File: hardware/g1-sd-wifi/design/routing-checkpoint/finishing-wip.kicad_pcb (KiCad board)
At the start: 6 copper layers, 59 x 115 mm, 351 parts, among them J10 FPGA JTAG pogo pads, J20 5V/GND direct wire pads, J201 microSD push-pull 1.42mm, J202 RP USB service pads, J203 RP SWD/reset/boot pads, J204 C5 direct UART recovery pads, J40 FH12-14S-0.5SH(55), J41 FH12-6S-0.5SH(55), J50 FH12-20S-0.5SH(55), J51 FH12-20S-0.5SH(55), K201 C5 removable compression cont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, K202 C5 removable compression cont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, K203 C5 removable compression cont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, K204 C5 removable compression cont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, K205 C5 removable compression cont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, K206 C5 removable compression cont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, K207 C5 removable compression cont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, K208 C5 removable compression cont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, K209 C5 removable compression cont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, K210 C5 removable compression cont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, K211 C5 removable compression cont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, K212 C5 removable compression cont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, K213 C5 removable compression cont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, K214 C5 removable compression cont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, K215 C5 removable compression cont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, K216 C5 removable compression cont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, Q20 PMV48XP reverse polarity, Q201 C5 recovery pull-down, Q202 C5 recovery pull-down, U10 LCMXO2-2000HC-4TG100C, U20 TPS2116 automatic mux, U201 RP2350B, U202 16MiB boot NOR, U203 8MiB QSPI PSRAM, U204 C5 off-state isolation, U205 C5 off-state isolation, U207 SD4-bit DAT rail isolation, U208 SD CLK/CMD rail isolation, U209 SD enable/power-good NAND, U21 TPS62162 3.3V 1A, U22 TPS62162 3.3V 1A, U23 TPS3808G33DBVR, U24 TPS3808G33DBVR, U25 TPS3808G33DBVR, U26 TPS3808G01DBVR, U27 SN74LVC2G08DCUR, U28 SN74LVC2G08DCUR, U29 SN74LVC2G08DCUR, U30 SN74LVC1G11DBVR, U31 SN74LVC2G04DBVT, U32 SN74LVC1G32DBVR, U33 SN74LVC1G08DBVR, U34 SN74LVC1G08DBVR, U35 SN74LVC16T245, U36 SN74LVC244A host controls, U37 SN74LVC1G17 host RESETn, U38 SN74LVC1G125 qualified ATA_IN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, U39 SN74LVC1G125 qualified ATA_DM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, U40 MX29LV640ETTI-70G x8 / 4 x 2M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, U41 SN74LVC2G125 bank-domain buff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, U42 SN74LVC1G11 write-authorize A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, U43 SN74LVC1G04 write-block inver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, U44 SN74LVC1G332 NOR WE qualifier, U45 TLV803EB29 console-rail NOR r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, U70 SN74LVC1G07 open-drain IORDY, U71 TPS22919 Wi-Fi input switch, U72 SN74LVC1G32DBVR, U73 SN74LVC1G32DBVR, X10 50MHz 3.3V, X201 12MHz

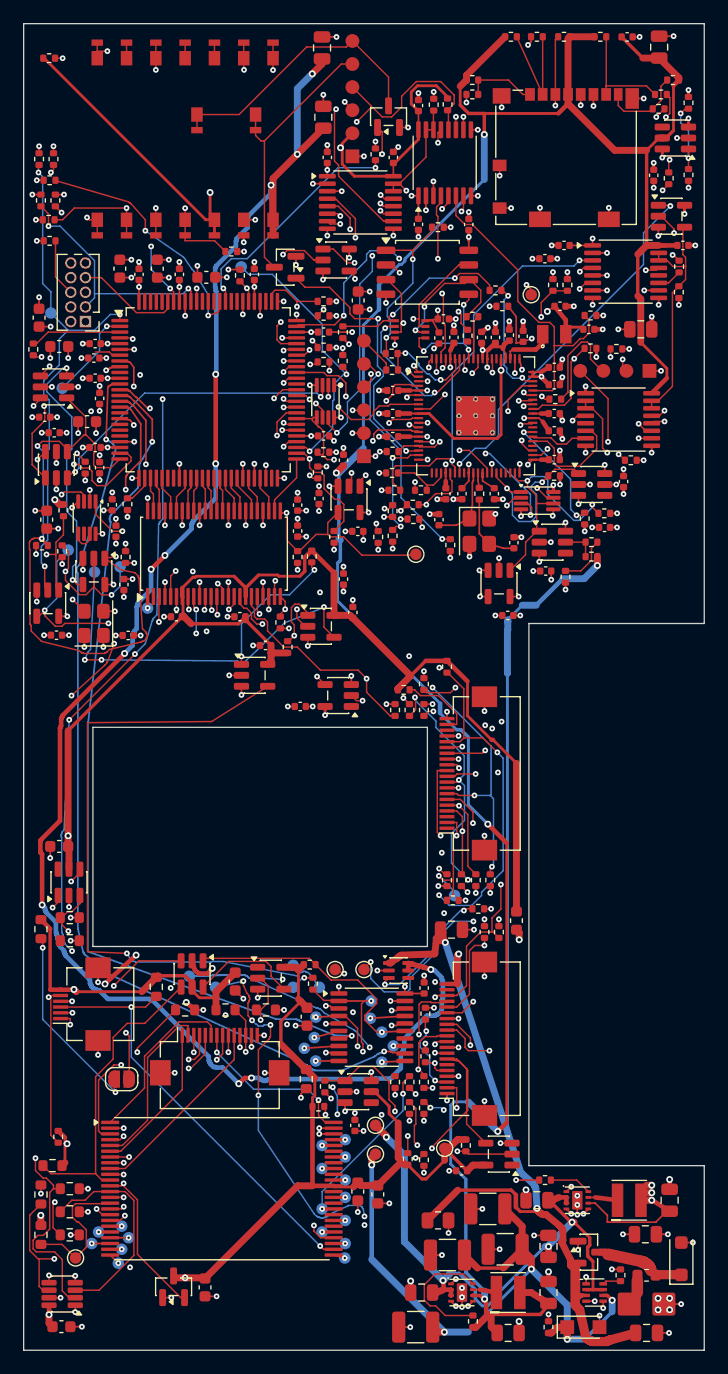
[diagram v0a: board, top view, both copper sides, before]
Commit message: G1 finishing: 19 open, supply current check passing; reroute rounds default to 3 passes
Co-Authored-By: Claude Opus 5.5 <noreply@anthropic.com>
Claude-Session: https://claude.ai/code/session_01Gp9EYc2r9fMpZ7V8WtfonZ
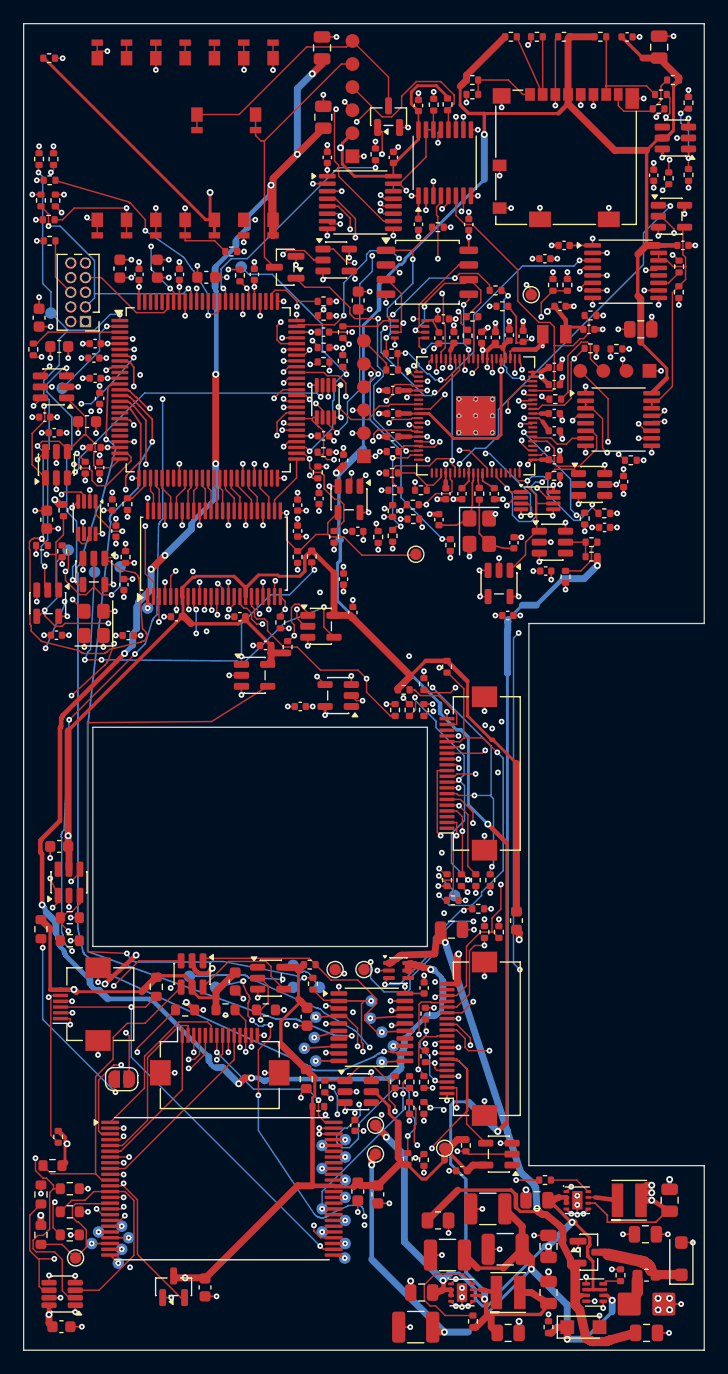
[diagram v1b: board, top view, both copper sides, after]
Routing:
- net ATA_DD0: track 31.0 -> 127.0 mm, vias 2 -> 5
- net BIOS_BANK0: track 19.7 -> 93.3 mm, vias 1 -> 3
- net BIOS_RECOVERYn: track 45.1 -> 80.2 mm, vias 3 -> 7
- net ATA_CS1n: track 12.0 -> 34.6 mm, vias 3 -> 4
- net INTRQ_OEn: track 63.4 -> 40.9 mm
- net +3V3_LOGIC: track 155.6 -> 158.6 mm
- net GND: track 252.1 -> 254.9 mm
- net ATA_DD8: track 45.5 -> 43.9 mm
- net HOST_OKn: track 69.4 -> 70.3 mm
- net RESERVE_5V: track 58.5 -> 59.1 mm

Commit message: G1 finishing: 18 open; gap closer lands on any point of the other copper island
- close_gaps.py: a connection may end anywhere on the island DRC's pair
  belongs to (tracks split exactly at the junction, so Freerouting sees
  it too); grid pitch configurable (KUI_GRID_MM) for 0.4 mm-pitch areas.
- reroute_finished.sh: UNLOCK and RIP_RADIUS options, PRIORITY override,
  a router stopped early still has its last session finished.
- force_supply_route.py: --signal lays boxed-in signal connections the
  same way, several nets per run.
- EDA-ENVIRONMENT: the healed round trip and the forcing tool.

Co-Authored-By: Claude Opus 5.5 <noreply@anthropic.com>
Claude-Session: https://claude.ai/code/session_01Gp9EYc2r9fMpZ7V8WtfonZ
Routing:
- net ATA_DD8: track 43.9 -> 172.6 mm, vias 3 -> 9
- net CONSOLE_3V3: track 290.4 -> 296.1 mm
- net GND: track 254.9 -> 253.2 mm
- net +3V3_LOGIC: track 158.6 -> 160.1 mm
- net BIOS_BANK0: track 93.3 -> 94.1 mm

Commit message: G1 finishing: 14 open; gap closer on a 0.025 mm grid during finishing
On the 0.05 mm grid the gap closer's quantisation margin added 0.05 mm
to the 0.127 mm clearance; between 0.4 mm-pitch pins that closed every
way. At 0.025 mm it joined four more (+1V1_MCU, REQ_DMARQ, ATA_DA0,
ATA_DD8). DRC 0, parity 0, supply current check passing.

Co-Authored-By: Claude Opus 5.5 <noreply@anthropic.com>
Claude-Session: https://claude.ai/code/session_01Gp9EYc2r9fMpZ7V8WtfonZ
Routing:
- net ATA_CS0n: track 9.70 -> 147.5 mm, vias 1 -> 9
- net ATA_DA0: track 38.0 -> 104.7 mm, vias 3 -> 10
- net REQ_DMARQ: track 19.9 -> 34.4 mm, vias 2 -> 5
- net +1V1_MCU: track 35.3 -> 45.7 mm, vias 2 -> 4
